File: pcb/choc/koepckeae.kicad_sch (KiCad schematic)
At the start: 50 parts, among them J1 Conn_01x09_Socket, J2 Conn_01x02_Socket, J3 Conn_01x02_Socket, J4 Conn_01x12_Socket, K1 PG1350, K10 PG1350, K11 PG1350, K12 PG1350, K13 PG1350, K14 PG1350, K15 PG1350, K16 PG1350, K17 PG1350, K18 PG1350, K19 PG1350, K2 PG1350, K20 PG1350, K21 PG1350, K22 PG1350, K23 PG1350, K24 PG1350, K25 PG1350, K26 PG1350, K27 PG1350, K28 PG1350, K29 PG1350, K3 PG1350, K30 PG1350, K31 PG1350, K32 PG1350, K33 PG1350, K34 PG1350, K4 PG1350, K5 PG1350, K6 PG1350, K7 PG1350, K8 PG1350, K9 PG1350, SW1 SW_Push, SW2 SW_SPDT, U1 Seeeduino Xiao nRF52840, U2 74HC595

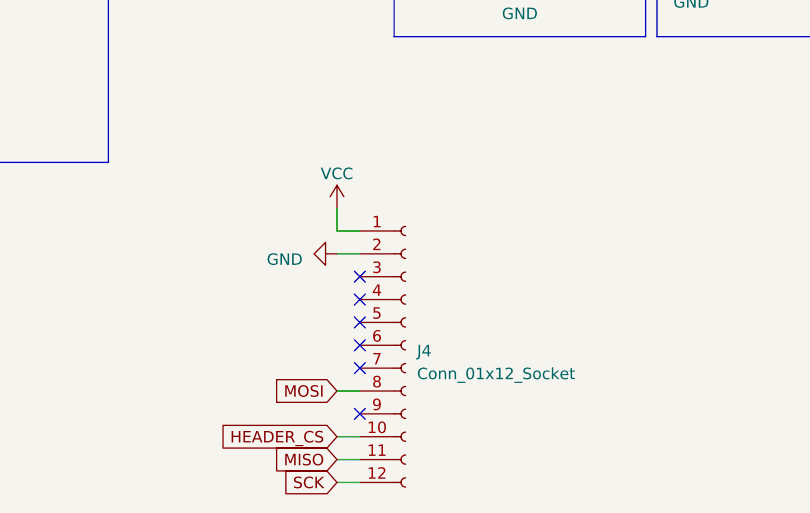
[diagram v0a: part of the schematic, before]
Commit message: Remove unused fpc
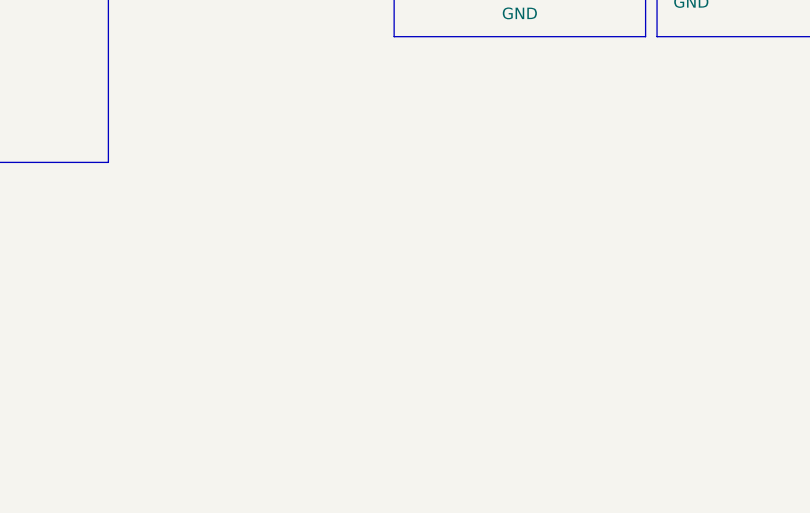
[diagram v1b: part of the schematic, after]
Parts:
- removed J4: Conn_01x12_Socket, Connector_FFC-FPC:Hirose_FH12-12S-0.5SH_1x12-1MP_P0.50mm_Horizontal, symbol Connector:Conn_01x12_Socket
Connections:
- no-connect marks 13 -> 7
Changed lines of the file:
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@@
   (no_connect (at 55.88 119.38))
   (no_connect (at 43.18 114.3))
-  (no_connect (at 143.51 177.8))
   (no_connect (at 102.87 139.7))
-  (no_connect (at 143.51 182.88))
   (no_connect (at 158.75 110.49))
   (no_connect (at 204.47 114.3))
   (no_connect (at 40.64 114.3))
-  (no_connect (at 143.51 167.64))
   (no_connect (at 48.26 114.3))
-  (no_connect (at 143.51 175.26))
-  (no_connect (at 143.51 172.72))
-  (no_connect (at 143.51 170.18))
   (wire (pts (xy 147.32 38.1) (xy 147.32 41.91))
     (stroke (width 0) (type default))
@@
     (stroke (width 0) (type default))
   )
-  (wire (pts (xy 140.97 190.5) (xy 143.51 190.5))
-    (stroke (width 0) (type default))
-  )
   (wire (pts (xy 107.95 87.63) (xy 107.95 90.17))
     (stroke (width 0) (type default))
@@
     (stroke (width 0) (type default))
   )
-  (wire (pts (xy 140.97 187.96) (xy 143.51 187.96))
-    (stroke (width 0) (type default))
-  )
   (wire (pts (xy 82.55 72.39) (xy 82.55 74.93))
     (stroke (width 0) (type default))
@@
     (stroke (width 0) (type default))
   )
-  (wire (pts (xy 140.97 160.02) (xy 140.97 162.56))
-    (stroke (width 0) (type default))
-  )
   (wire (pts (xy 48.26 68.58) (xy 50.8 68.58))
     (stroke (width 0) (type default))
@@
     (stroke (width 0) (type default))
   )
-  (wire (pts (xy 143.51 162.56) (xy 140.97 162.56))
-    (stroke (width 0) (type default))
-  )
   (wire (pts (xy 91.44 68.58) (xy 91.44 72.39))
     (stroke (width 0) (type default))
@@
     (stroke (width 0) (type default))
   )
-  (wire (pts (xy 140.97 185.42) (xy 143.51 185.42))
-    (stroke (width 0) (type default))
-  )
   (wire (pts (xy 97.79 90.17) (xy 107.95 90.17))
     (stroke (width 0) (type default))
@@
     (stroke (width 0) (type default))
   )
-  (wire (pts (xy 140.97 180.34) (xy 143.51 180.34))
-    (stroke (width 0) (type default))
-  )
   (wire (pts (xy 45.72 57.15) (xy 44.45 57.15))
     (stroke (width 0) (type default))
@@
   )
   (wire (pts (xy 67.31 90.17) (xy 82.55 90.17))
-    (stroke (width 0) (type default))
-  )
-  (wire (pts (xy 140.97 165.1) (xy 143.51 165.1))
     (stroke (width 0) (type default))
   )
@@
     )
   )
-  (global_label "SCK" (shape input) (at 140.97 190.5 180) (fields_autoplaced)
-    (effects (font (size 1.27 1.27)) (justify right))
-    (property "Intersheetrefs" "${INTERSHEET_REFS}" (at 134.3147 190.5 0)
-      (effects (font (size 1.27 1.27)) (justify right) hide)
-    )
-  )
   (global_label "HEADER_CS" (shape input) (at 27.94 134.62 180) (fields_autoplaced)
     (effects (font (size 1.27 1.27)) (justify right))
@@
     )
   )
-  (global_label "MISO" (shape input) (at 140.97 187.96 180) (fields_autoplaced)
-    (effects (font (size 1.27 1.27)) (justify right))
-    (property "Intersheetrefs" "${INTERSHEET_REFS}" (at 133.468 187.96 0)
-      (effects (font (size 1.27 1.27)) (justify right) hide)
-    )
-  )
   (global_label "MOSI" (shape input) (at 163.83 120.65 0) (fields_autoplaced)
     (effects (font (size 1.27 1.27)) (justify left))
@@
     )
   )
-  (global_label "HEADER_CS" (shape input) (at 140.97 185.42 180) (fields_autoplaced)
-    (effects (font (size 1.27 1.27)) (justify right))
-    (property "Intersheetrefs" "${INTERSHEET_REFS}" (at 127.36 185.42 0)
-      (effects (font (size 1.27 1.27)) (justify right) hide)
-    )
-  )
   (global_label "P009" (shape input) (at 163.83 130.81 0) (fields_autoplaced)
     (effects (font (size 1.27 1.27)) (justify left))
@@
     (property "Intersheetrefs" "${INTERSHEET_REFS}" (at 48.26 22.7361 90)
       (effects (font (size 1.27 1.27)) (justify left) hide)
-    )
-  )
-  (global_label "MOSI" (shape input) (at 140.97 180.34 180) (fields_autoplaced)
-    (effects (font (size 1.27 1.27)) (justify right))
-    (property "Intersheetrefs" "${INTERSHEET_REFS}" (at 133.468 180.34 0)
-      (effects (font (size 1.27 1.27)) (justify right) hide)
     )
   )
@@
         (path "/84582659-f20d-4b57-a904-d4b599b50d46"
           (reference "K34") (unit 1)
-        )
-      )
-    )
-  )
-  (symbol (lib_id "power:GND") (at 140.97 165.1 270) (unit 1)
-    (in_bom yes) (on_board yes) (dnp no) (fields_autoplaced)
-    (property "Reference" "#PWR012" (at 134.62 165.1 0)
-      (effects (font (size 1.27 1.27)) hide)
-    )
-    (property "Value" "GND" (at 137.16 165.735 90)
-      (effects (font (size 1.27 1.27)) (justify right))
-    )
-    (property "Footprint" "" (at 140.97 165.1 0)
-      (effects (font (size 1.27 1.27)) hide)
-    )
-    (property "Datasheet" "" (at 140.97 165.1 0)
-      (effects (font (size 1.27 1.27)) hide)
-    )
-    (pin "1")
-    (instances
-      (project "koepckeae"
-        (path "/84582659-f20d-4b57-a904-d4b599b50d46"
-          (reference "#PWR012") (unit 1)
         )
       )
@@
     )
   )
-  (symbol (lib_id "power:VCC") (at 140.97 160.02 0) (unit 1)
-    (in_bom yes) (on_board yes) (dnp no) (fields_autoplaced)
-    (property "Reference" "#PWR011" (at 140.97 163.83 0)
-      (effects (font (size 1.27 1.27)) hide)
-    )
-    (property "Value" "VCC" (at 140.97 156.21 0)
-      (effects (font (size 1.27 1.27)))
-    )
-    (property "Footprint" "" (at 140.97 160.02 0)
-      (effects (font (size 1.27 1.27)) hide)
-    )
-    (property "Datasheet" "" (at 140.97 160.02 0)
-      (effects (font (size 1.27 1.27)) hide)
-    )
-    (pin "1")
-    (instances
-      (project "koepckeae"
-        (path "/84582659-f20d-4b57-a904-d4b599b50d46"
-          (reference "#PWR011") (unit 1)
-        )
-      )
-    )
-  )
   (symbol (lib_id "koepckeae:PG1350") (at 71.12 48.26 0) (unit 1)
     (in_bom yes) (on_board yes) (dnp no) (fields_autoplaced)
@@
         )
       )
-    )
-  )
-  (symbol (lib_id "Connector:Conn_01x12_Socket") (at 148.59 175.26 0) (unit 1)
-    (in_bom yes) (on_board yes) (dnp no) (fields_autoplaced)
-    (property "Reference" "J4" (at 149.86 175.895 0)
-      (effects (font (size 1.27 1.27)) (justify left))
-    )
-    (property "Value" "Conn_01x12_Socket" (at 149.86 178.435 0)
-      (effects (font (size 1.27 1.27)) (justify left))
-    )
-    (property "Footprint" "Connector_FFC-FPC:Hirose_FH12-12S-0.5SH_1x12-1MP_P0.50mm_Horizontal" (at 148.59 175.26 0)
-      (effects (font (size 1.27 1.27)) hide)
-    )
-    (property "Datasheet" "~" (at 148.59 175.26 0)
-      (effects (font (size 1.27 1.27)) hide)
-    )
-    (pin "1")
-    (pin "10")
-    (pin "11")
-    (pin "12")
-    (pin "2")
-    (pin "3")
-    (pin "4")
-    (pin "5")
-    (pin "6")
-    (pin "7")
-    (pin "8")
-    (pin "9")
-    (instances
-      (project "koepckeae"
-        (path "/84582659-f20d-4b57-a904-d4b599b50d46"
-          (reference "J4") (unit 1)
-        )
-      )
